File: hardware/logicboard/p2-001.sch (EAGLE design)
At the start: 32 parts, among them IC1 5V, IC2 74LS07N, IC3 4066N, IC4 LTC485N, K1 G5V1, T1 2SC1815, U1 DS18B20

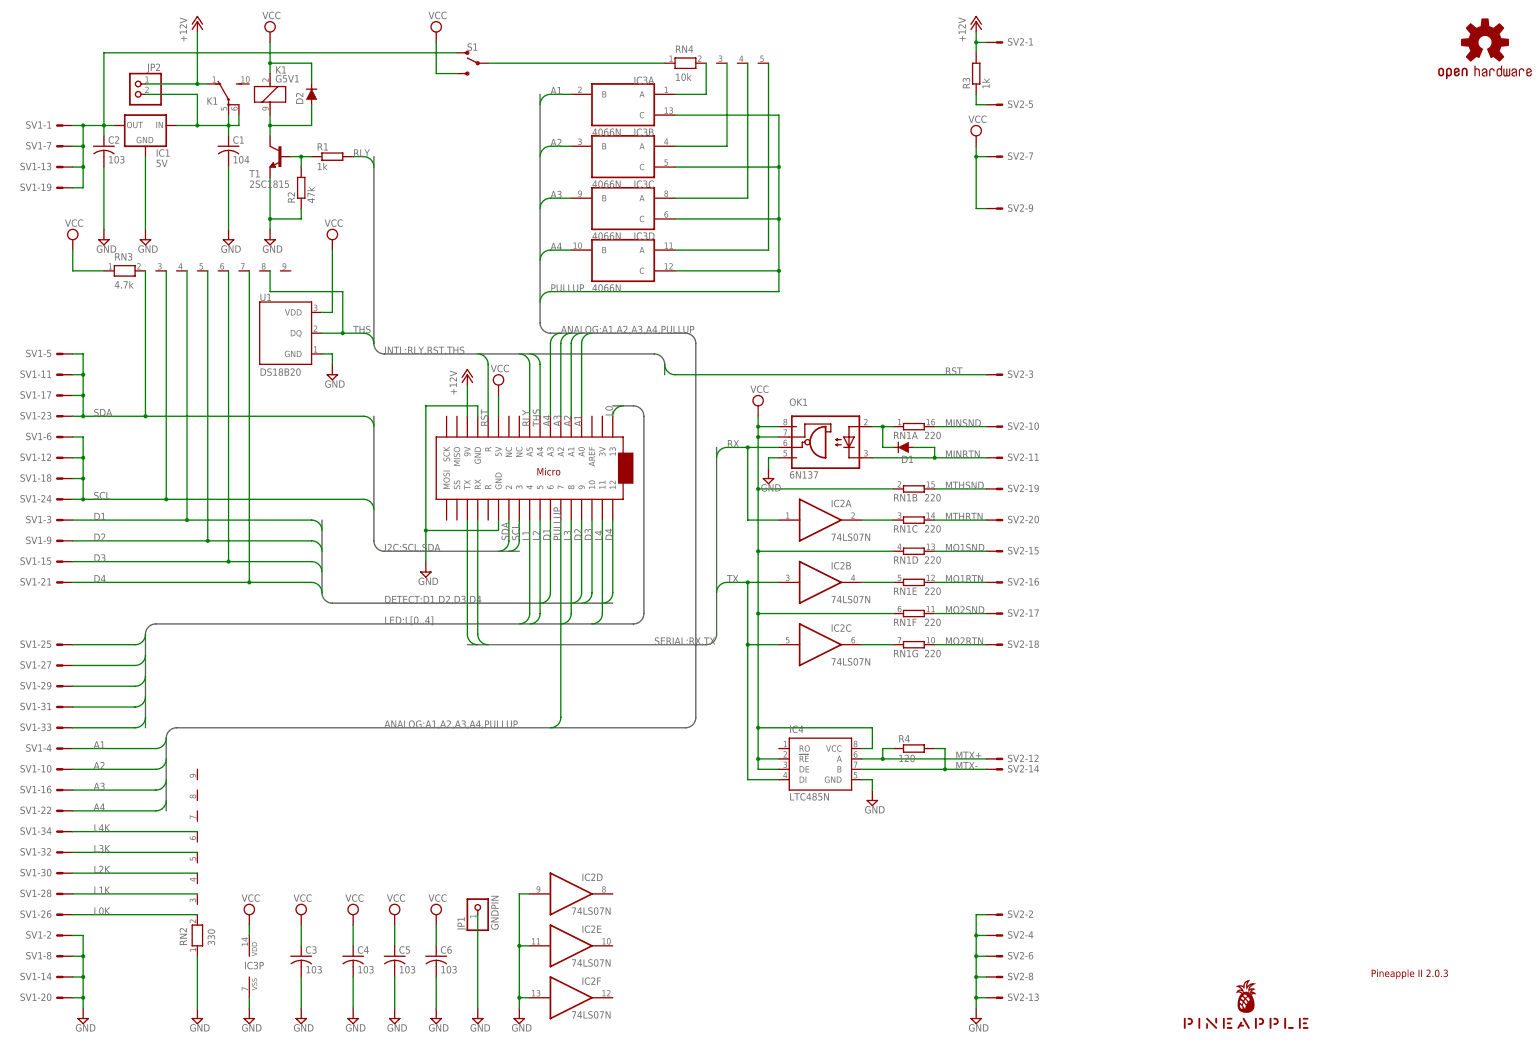
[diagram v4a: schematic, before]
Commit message: Back LED is now connected to D13 (again).
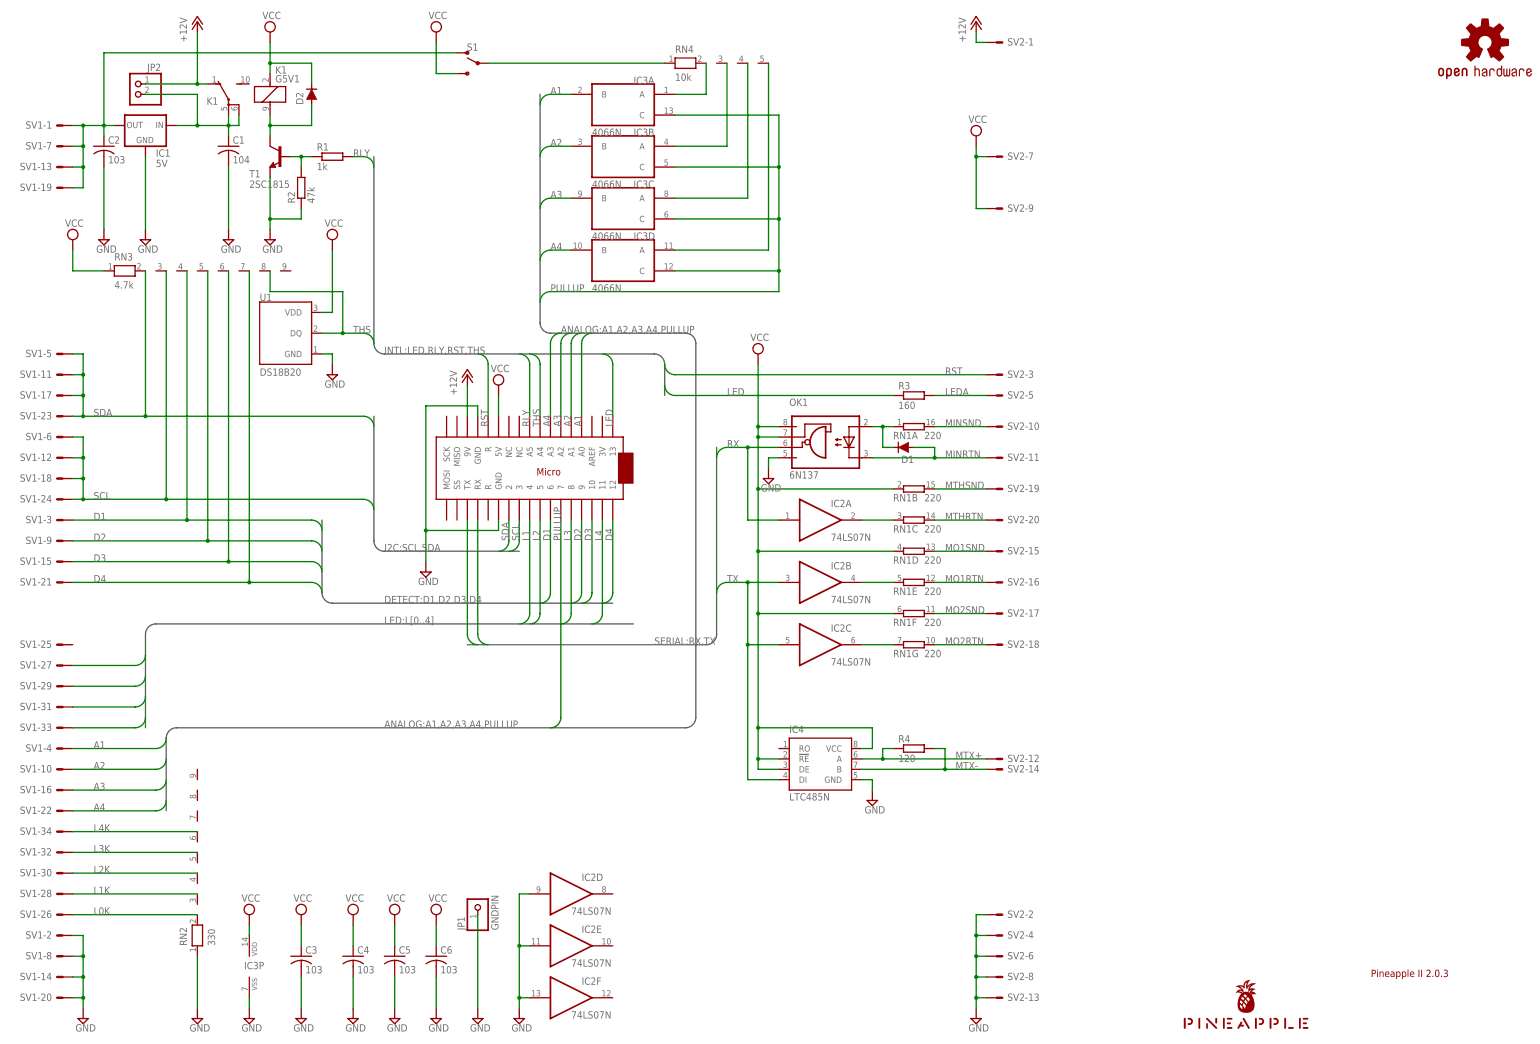
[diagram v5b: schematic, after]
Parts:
- R3: value 1k -> 160
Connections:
- removed net L0: MC1.13, SV1-25.S
- removed net PWRLED: R3.1, SV2-5.S
- new net LED: MC1.13, R3.1
- new net LEDA: R3.2, SV2-5.S
- net VIN: no longer R3.2
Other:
- moved on the sheet: R3, SV2-5
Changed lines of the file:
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@@
 <part name="SUPPLY5" library="supply2" library_urn="urn:adsk.eagle:library:372" deviceset="VCC" device=""/>
 <part name="S1" library="SparkFun-Switches" deviceset="SWITCH-SPDT" device="-PTH-11.6X4.0MM"/>
-<part name="R3" library="resistor" library_urn="urn:adsk.eagle:library:348" deviceset="R-EU_" device="0204/5" package3d_urn="urn:adsk.eagle:package:23488/1" value="1k"/>
+<part name="R3" library="resistor" library_urn="urn:adsk.eagle:library:348" deviceset="R-EU_" device="0204/5" package3d_urn="urn:adsk.eagle:package:23488/1" value="160"/>
 <part name="SUPPLY24" library="supply2" deviceset="GND" device=""/>
 <part name="IC4" library="linear-technology" library_urn="urn:adsk.eagle:library:261" deviceset="LTC485" device="N" package3d_urn="urn:adsk.eagle:package:29519/2"/>
@@
 <attribute name="VALUE" x="200.66" y="142.24" size="1.778" layer="96"/>
 </instance>
-<instance part="SUPPLY19" gate="G$1" x="193.04" y="160.02" smashed="yes">
-<attribute name="VALUE" x="191.135" y="163.195" size="1.778" layer="96"/>
+<instance part="SUPPLY19" gate="G$1" x="193.04" y="172.72" smashed="yes">
+<attribute name="VALUE" x="191.135" y="175.895" size="1.778" layer="96"/>
 </instance>
 <instance part="D1" gate="G$1" x="228.6" y="149.86" smashed="yes" rot="R180">
@@
 <attribute name="VALUE" x="251.206" y="27.559" size="1.778" layer="96"/>
 </instance>
-<instance part="SV2" gate="-5" x="251.46" y="233.68" smashed="yes">
-<attribute name="NAME" x="254" y="232.918" size="1.778" layer="95"/>
-<attribute name="VALUE" x="251.206" y="230.759" size="1.778" layer="96"/>
+<instance part="SV2" gate="-5" x="251.46" y="162.56" smashed="yes">
+<attribute name="NAME" x="254" y="161.798" size="1.778" layer="95"/>
+<attribute name="VALUE" x="251.206" y="159.639" size="1.778" layer="96"/>
 </instance>
 <instance part="SV2" gate="-6" x="251.46" y="25.4" smashed="yes">
@@
 <attribute name="VALUE" x="123.444" y="240.538" size="1.778" layer="96" font="vector" rot="MR0" align="top-center"/>
 </instance>
-<instance part="R3" gate="G$1" x="246.38" y="241.3" smashed="yes" rot="R90">
-<attribute name="NAME" x="244.8814" y="237.49" size="1.778" layer="95" rot="R90"/>
-<attribute name="VALUE" x="249.682" y="237.49" size="1.778" layer="96" rot="R90"/>
+<instance part="R3" gate="G$1" x="231.14" y="162.56" smashed="yes">
+<attribute name="NAME" x="227.33" y="164.0586" size="1.778" layer="95"/>
+<attribute name="VALUE" x="227.33" y="159.258" size="1.778" layer="96"/>
 </instance>
 <instance part="SUPPLY24" gate="GND" x="134.62" y="10.16" smashed="yes">
@@
 <bus name="LED:L[0..4]">
 <segment>
-<wire x1="162.56" y1="106.68" x2="165.1" y2="109.22" width="0.762" layer="92" curve="90"/>
-<wire x1="165.1" y1="109.22" x2="165.1" y2="157.48" width="0.762" layer="92"/>
-<wire x1="165.1" y1="157.48" x2="162.56" y2="160.02" width="0.762" layer="92" curve="90"/>
-<wire x1="162.56" y1="160.02" x2="157.48" y2="160.02" width="0.762" layer="92"/>
 <wire x1="162.56" y1="106.68" x2="45.72" y2="106.68" width="0.762" layer="92"/>
 <label x="101.6" y="106.68" size="1.778" layer="95"/>
@@
 </segment>
 </bus>
-<bus name="INTL:RLY,RST,THS">
+<bus name="INTL:LED,RLY,RST,THS">
 <segment>
 <wire x1="167.64" y1="172.72" x2="101.6" y2="172.72" width="0.762" layer="92"/>
@@
 <label x="101.6" y="172.72" size="1.778" layer="95"/>
 <wire x1="167.64" y1="172.72" x2="170.18" y2="170.18" width="0.762" layer="92" curve="-90"/>
-<wire x1="170.18" y1="170.18" x2="170.18" y2="167.64" width="0.762" layer="92"/>
+<wire x1="170.18" y1="170.18" x2="170.18" y2="162.56" width="0.762" layer="92"/>
 </segment>
 </bus>
@@
 <segment>
 <pinref part="SUPPLY19" gate="G$1" pin="VCC"/>
-<wire x1="193.04" y1="157.48" x2="193.04" y2="154.94" width="0.1524" layer="91"/>
+<wire x1="193.04" y1="170.18" x2="193.04" y2="154.94" width="0.1524" layer="91"/>
 <pinref part="OK1" gate="A" pin="VE"/>
 <wire x1="193.04" y1="154.94" x2="193.04" y2="152.4" width="0.1524" layer="91"/>
@@
 <pinref part="SV2" gate="-1" pin="S"/>
 <wire x1="246.38" y1="248.92" x2="248.92" y2="248.92" width="0.1524" layer="91"/>
-<pinref part="R3" gate="G$1" pin="2"/>
-<wire x1="246.38" y1="248.92" x2="246.38" y2="246.38" width="0.1524" layer="91"/>
-<junction x="246.38" y="248.92"/>
 </segment>
 <segment>
@@
 </segment>
 </net>
-<net name="PWRLED" class="0">
-<segment>
-<pinref part="R3" gate="G$1" pin="1"/>
-<wire x1="246.38" y1="236.22" x2="246.38" y2="233.68" width="0.1524" layer="91"/>
-<pinref part="SV2" gate="-5" pin="S"/>
-<wire x1="246.38" y1="233.68" x2="248.92" y2="233.68" width="0.1524" layer="91"/>
-</segment>
-</net>
 <net name="MTHSND" class="0">
 <segment>
@@
 </segment>
 </net>
-<net name="L0" class="0">
+<net name="LED" class="0">
 <segment>
 <pinref part="MC1" gate="G$1" pin="13"/>
-<wire x1="160.02" y1="160.02" x2="157.48" y2="157.48" width="0.1524" layer="91" curve="90"/>
-<label x="157.48" y="157.48" size="1.778" layer="95" rot="R90"/>
-</segment>
-<segment>
-<pinref part="SV1" gate="-25" pin="S"/>
-<wire x1="43.18" y1="104.14" x2="40.64" y2="101.6" width="0.1524" layer="91" curve="-90"/>
-<wire x1="40.64" y1="101.6" x2="25.4" y2="101.6" width="0.1524" layer="91"/>
-</segment>
-</net>
+<wire x1="154.94" y1="172.72" x2="157.48" y2="170.18" width="0.1524" layer="91" curve="-90"/>
+<wire x1="157.48" y1="170.18" x2="157.48" y2="157.48" width="0.1524" layer="91"/>
+<label x="157.48" y="154.94" size="1.778" layer="95" rot="R90"/>
+</segment>
+<segment>
+<pinref part="R3" gate="G$1" pin="1"/>
+<wire x1="170.18" y1="165.1" x2="172.72" y2="162.56" width="0.1524" layer="91" curve="90"/>
+<wire x1="172.72" y1="162.56" x2="226.06" y2="162.56" width="0.1524" layer="91"/>
+<label x="185.42" y="162.56" size="1.778" layer="95"/>
+</segment>
+</net>
+<net name="LEDA" class="0">
+<segment>
+<pinref part="R3" gate="G$1" pin="2"/>
+<pinref part="SV2" gate="-5" pin="S"/>
+<wire x1="236.22" y1="162.56" x2="248.92" y2="162.56" width="0.1524" layer="91"/>
+<label x="238.76" y="162.56" size="1.778" layer="95"/>
+</segment>
+</net>

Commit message: More change.
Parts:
- removed RN4: 10k, resistor-net:RN04
- added J1: (no value), SparkFun-Connectors:CONN_05JST
- added R5: 160, resistor:R-EU_0204/5
- JP1: value GNDPIN -> PWR; device pinhead:PINHD-1X1 -> pinhead:PINHD-1X3
- R3: value 160 -> 120
- R4: value 120 -> 160
- RN2: value 330 -> 4.7k
- RN3: value 4.7k -> 10k; device resistor-net:RN08 -> resistor-net:RN04
- SV1: device con-ml:ML34LE -> con-ml:ML26LE
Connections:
- net VIN renamed +12V
- removed net L0K: RN2.2, SV1-26.S
- removed net L1: MC1.4, SV1-27.S
- removed net L1K: RN2.3, SV1-28.S
- removed net L2: MC1.5, SV1-29.S
- removed net L2K: RN2.4, SV1-30.S
- removed net L3: MC1.8, SV1-31.S
- removed net L3K: RN2.5, SV1-32.S
- removed net L4: MC1.11, SV1-33.S
- removed net L4K: RN2.6, SV1-34.S
- new net FLED: MC1.11, SV1-25.S
- new net GPIO1: J1.3, MC1.4
- new net GPIO2: J1.4, MC1.5
- new net GPIO3: J1.5, MC1.8
- new net MOSI: J1.1, MC1.MOSI
- new net N$1: R5.2, SV1-26.S
- new net SCLK: J1.2, MC1.SCK
- new net VDD: JP1.3, MC1.3V
- net D1: now also RN2.4; no longer RN3.4
- net D2: now also RN2.5; no longer RN3.5
- net D3: now also RN2.6; no longer RN3.6
- net D4: now also RN2.7; no longer RN3.7
- net GND: now also JP1.2, R5.1; no longer JP1.1, RN2.1
- net LED: now also R4.1; no longer R3.1
- net LEDA: now also R4.2; no longer R3.2
- net MTX+: now also R3.1; no longer R4.1
- net MTX-: now also R3.2; no longer R4.2
- net N$3: now also RN3.2; no longer RN4.2
- net N$4: now also RN3.3; no longer RN4.3
- net N$5: now also RN3.4; no longer RN4.4
- net N$6: now also RN3.5; no longer RN4.5
- net SCL: now also RN2.3; no longer RN3.3
- net SDA: now also RN2.2; no longer RN3.2
- net THS: now also RN2.8; no longer RN3.8
- net VCC: now also JP1.1, RN2.1; no longer RN3.1
- net VPULLUP: now also RN3.1; no longer RN4.1
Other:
- moved on the sheet: R3, R4, RN2, SV1-10, SV1-16, SV1-22, SV1-25, SV1-26, SV1-4
